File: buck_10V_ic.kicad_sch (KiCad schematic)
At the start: 29 parts, among them U3701 SIC462ED-T1-GE3

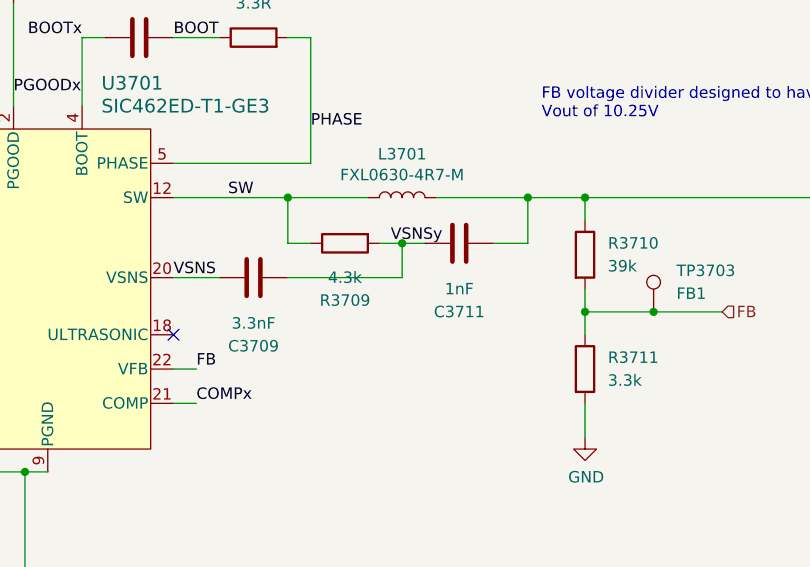
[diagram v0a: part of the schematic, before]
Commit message: Update buck components according to testing results
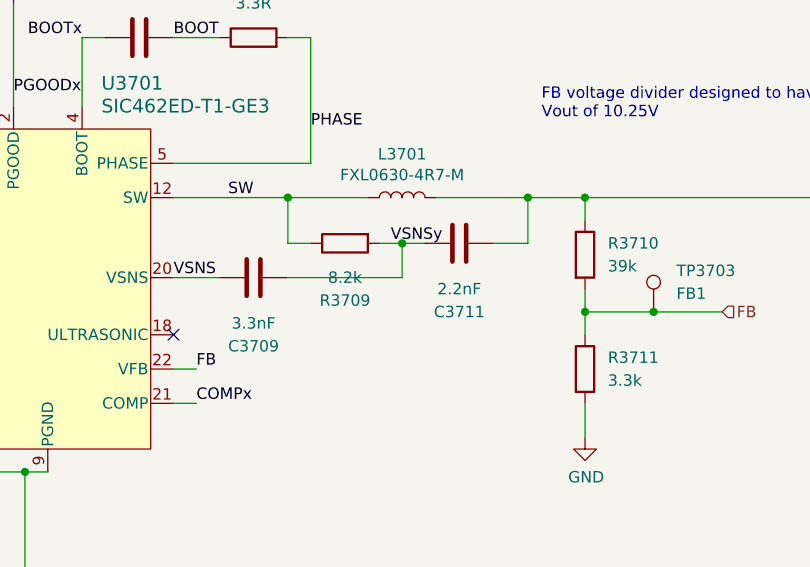
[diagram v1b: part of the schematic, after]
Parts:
- C3711: value 1nF -> 2.2nF; LCSC C1588 -> (none)
- R3709: value 4.3k -> 8.2k; LCSC C23159 -> (none)
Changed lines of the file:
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@@
 			)
 		)
-		(property "Value" "1nF"
+		(property "Value" "2.2nF"
 			(at 181.61 95.25 90)
 			(effects
@@
 			)
 		)
-		(property "LCSC" "C1588"
+		(property "LCSC" ""
 			(at 181.61 90.17 0)
 			(effects
@@
 			)
 		)
-		(property "Value" "4.3k"
+		(property "Value" "8.2k"
 			(at 168.91 93.98 90)
 			(effects
@@
 			)
 		)
-		(property "LCSC" "C23159"
+		(property "LCSC" ""
 			(at 168.91 90.17 0)
 			(effects

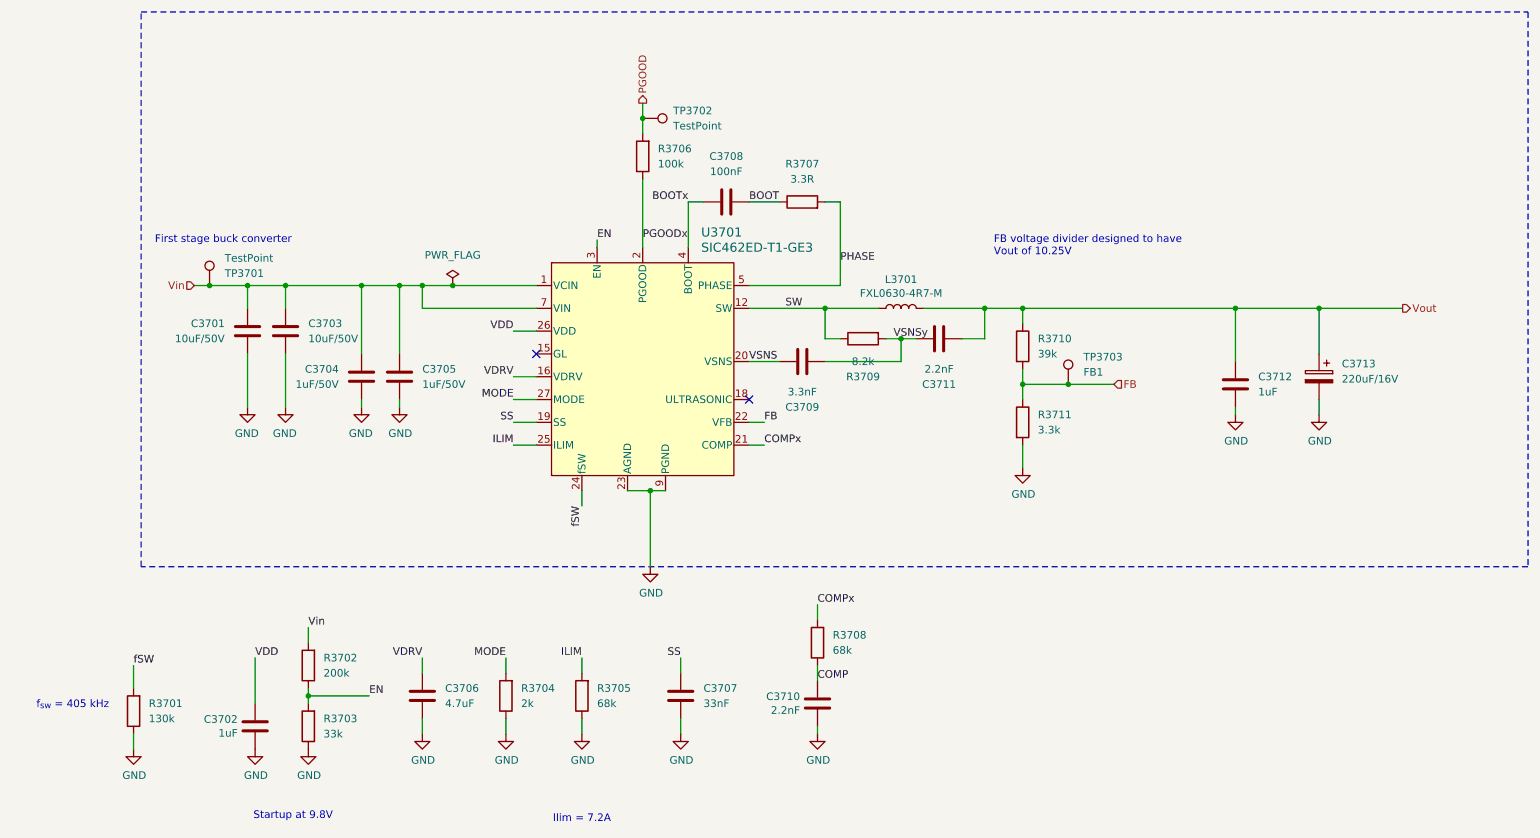
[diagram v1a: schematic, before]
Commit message: Get the buck EN input from VIN_OVP
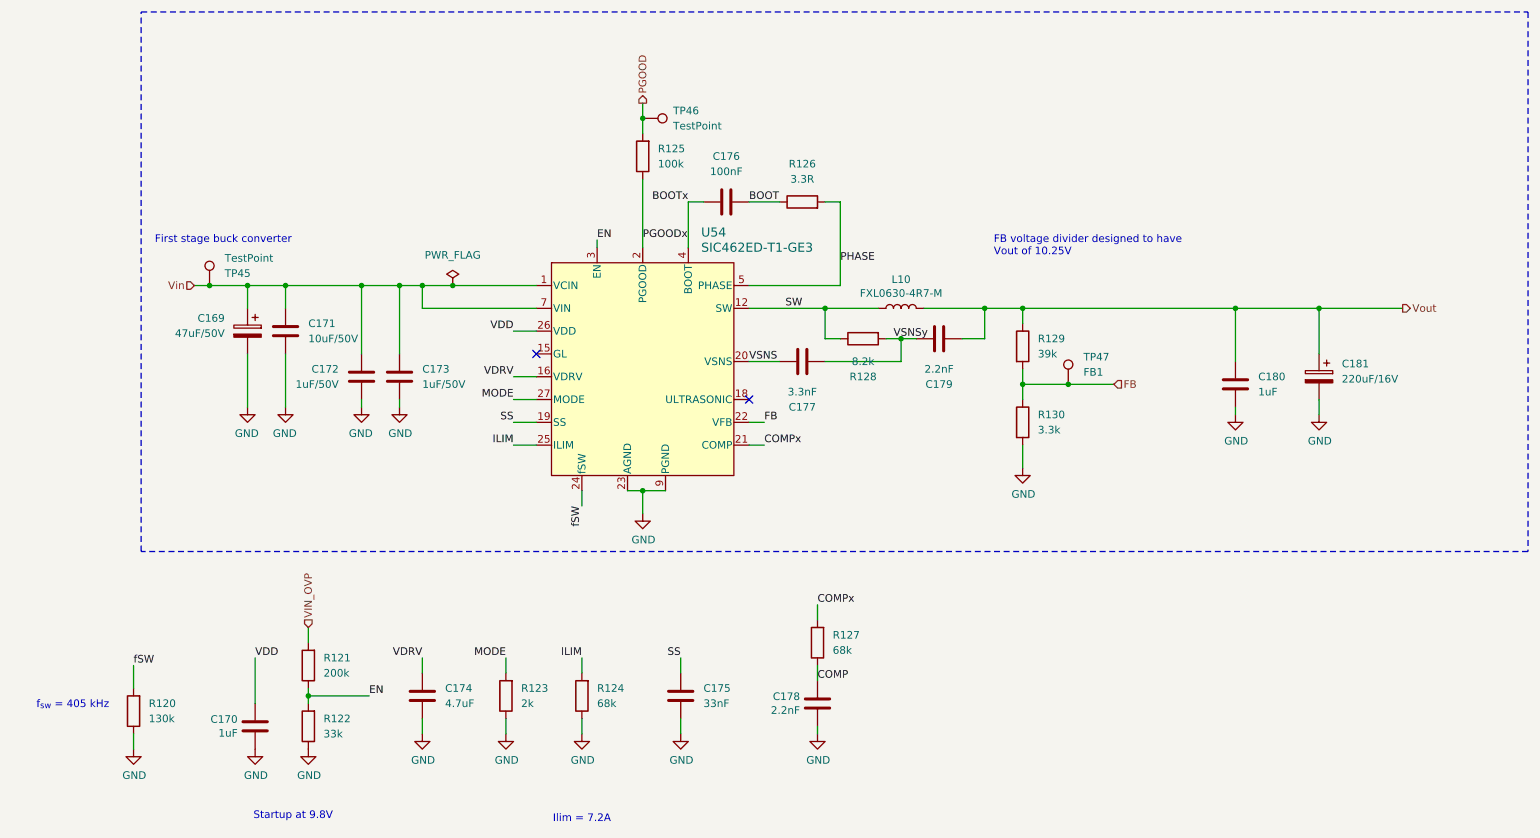
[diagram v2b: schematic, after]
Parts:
- removed C3701: 10uF/50V, Capacitor_SMD:C_1206_3216Metric, symbol Device:C
- added C169: 47uF/50V, symbol Device:C_Polarized
- C179: renamed from C3711; LCSC (none) -> C1604
- R128: renamed from R3709; LCSC (none) -> C25981
- renumbered C3702 to C170, C3703 to C171, C3704 to C172, C3705 to C173, C3706 to C174, C3707 to C175, C3708 to C176, C3709 to C177, C3710 to C178, C3712 to C180, C3713 to C181, L3701 to L10, R3701 to R120, R3702 to R121, R3703 to R122, R3704 to R123, R3705 to R124, R3706 to R125, R3707 to R126, R3708 to R127, R3710 to R129, R3711 to R130, TP3701 to TP45, TP3702 to TP46, TP3703 to TP47, U3701 to U54
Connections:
- net GND: now also C169.2
- net Vin: now also C169.1; no longer R121.2
- new net VIN_OVP: R121.2

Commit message: Reannotate the board
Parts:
- renumbered C169 to C170, C170 to C171, C171 to C172, C172 to C173, C173 to C174, C174 to C175, C175 to C176, C176 to C177, C177 to C178, C178 to C179, C179 to C180, C180 to C181, C181 to C182, TP45 to TP44, TP46 to TP45, TP47 to TP46, U54 to U53

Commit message: Fix DRC issues
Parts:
- removed C173: 1uF/50V, Capacitor_SMD:C_0603_1608Metric, symbol Device:C
- added C187: 1uF/50V, Capacitor_SMD:C_0603_1608Metric, symbol Device:C
- added C188: 1nF, Capacitor_SMD:C_0603_1608Metric, symbol Device:C
- added R135: 0R, Resistor_SMD:R_0603_1608Metric, symbol Device:R
- C170: footprint (none) -> Capacitor_SMD:CP_Elec_6.3x7.7; LCSC (none) -> C44606723
- C176: value 33nF -> 100nF; LCSC 0603 -> C14663
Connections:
- net GND: now also C187.2, C188.2
- net SW: now also R135.2
- net Vin: now also C187.1
- new net SNUB_: C188.1, R135.1
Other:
- note added: "Power save enabled, internal regulator enabled"
- note added: "Snubber circuit"
- note added: "Soft start time about 16 ms"
- moved on the sheet: C170, C172, C174, TP44

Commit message: Add GND/3.3V/5V headers, add missing JLC part numbers
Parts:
- C188: LCSC (none) -> C1588
- R135: LCSC (none) -> C21189
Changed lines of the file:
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@@
 	(wire
 		(pts
-			(xy 149.86 85.09) (xy 162.56 85.09)
+			(xy 92.71 81.28) (xy 100.33 81.28)
 		)
 		(stroke
@@
 	(wire
 		(pts
-			(xy 92.71 81.28) (xy 100.33 81.28)
+			(xy 149.86 85.09) (xy 162.56 85.09)
 		)
 		(stroke
@@
 			)
 		)
-		(property "LCSC" ""
+		(property "LCSC" "C1588"
 			(at 180.34 148.59 0)
 			(effects
@@
 			)
 		)
-		(property "LCSC" ""
+		(property "LCSC" "C21189"
 			(at 180.34 138.43 0)
 			(effects

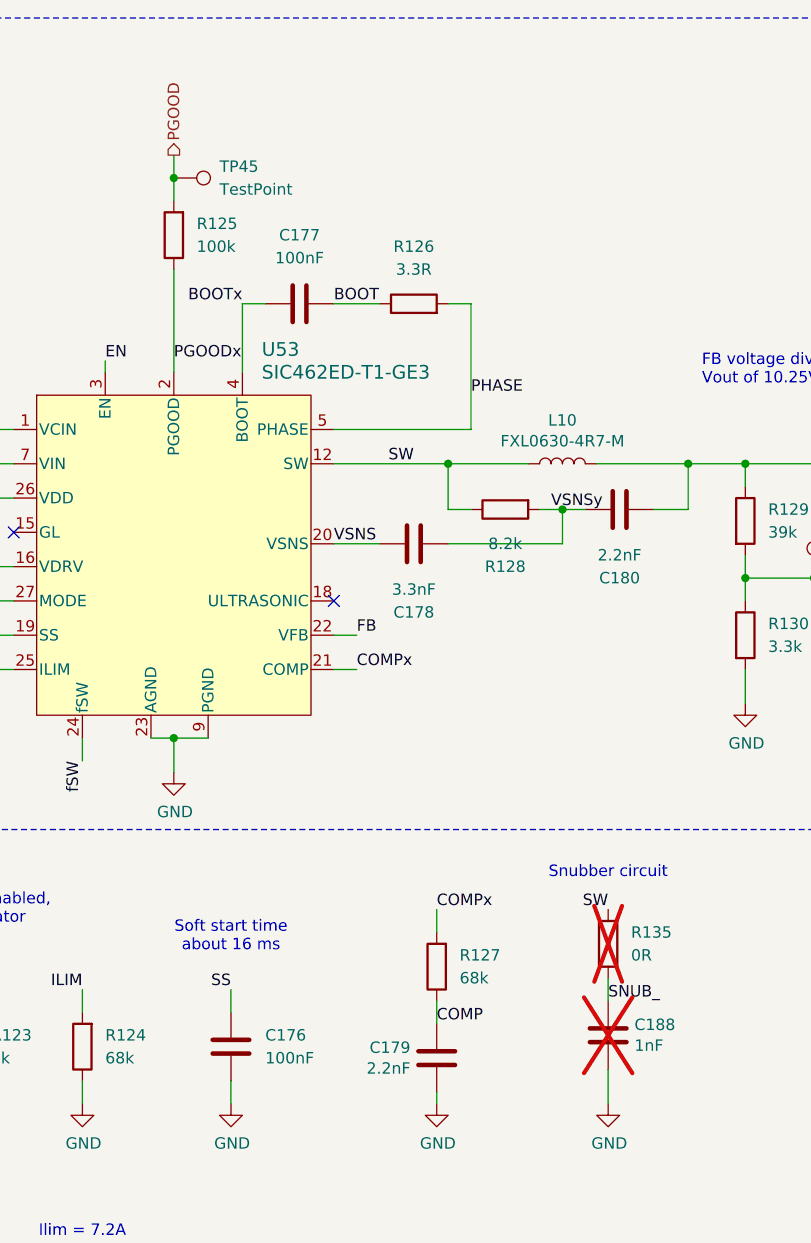
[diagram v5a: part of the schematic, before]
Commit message: Adjust 10V buck design based on Vishay tool output
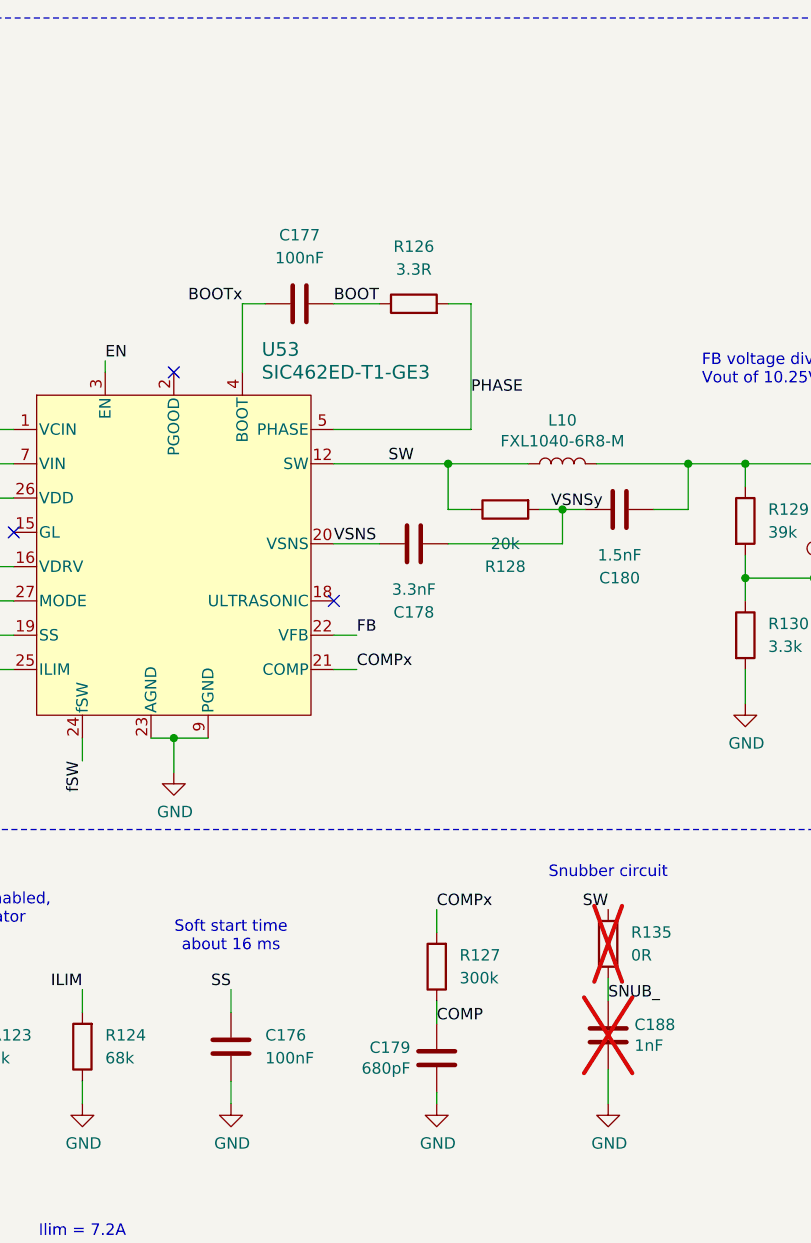
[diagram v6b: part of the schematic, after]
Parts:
- removed R125: 100k, Resistor_SMD:R_0402_1005Metric, symbol Device:R
- removed TP45: TestPoint, TestPoint:TestPoint_Pad_D1.0mm, symbol Connector:TestPoint
- C179: value 2.2nF -> 680pF; LCSC C1604 -> C1630
- C180: value 2.2nF -> 1.5nF; LCSC C1604 -> C1595
- L10: value FXL0630-4R7-M -> FXL1040-6R8-M; footprint Inductor_SMD:L_Changjiang_FXL0630 -> Inductor_SMD:L_Changjiang_FXL1040; LCSC C167220 -> C167231
- R127: value 68k -> 300k; LCSC C23231 -> C23024
- R128: value 8.2k -> 20k; LCSC C25981 -> C4184
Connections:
- net PGOODx: no longer names the net of U53.2 (PGOOD)
- no-connect marks 2 -> 3

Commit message: FInal v0.2.0 proto changes
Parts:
- R129: LCSC C25783 -> C23153
- renumbered C170 to C172, C171 to C173, C172 to C174, C187 to C175, C174 to C176, C175 to C177, C176 to C178, C177 to C179, C178 to C180, C179 to C181, C188 to C182, C180 to C183, C181 to C184, C182 to C185, R126 to R125, R127 to R126, R128 to R127, R135 to R128, TP44 to TP81, TP46 to TP82
